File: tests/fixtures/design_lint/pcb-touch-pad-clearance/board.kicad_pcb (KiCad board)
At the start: 2 copper layers, 20 x 20 mm, 1 part, among them J1 Synthetic_Connector

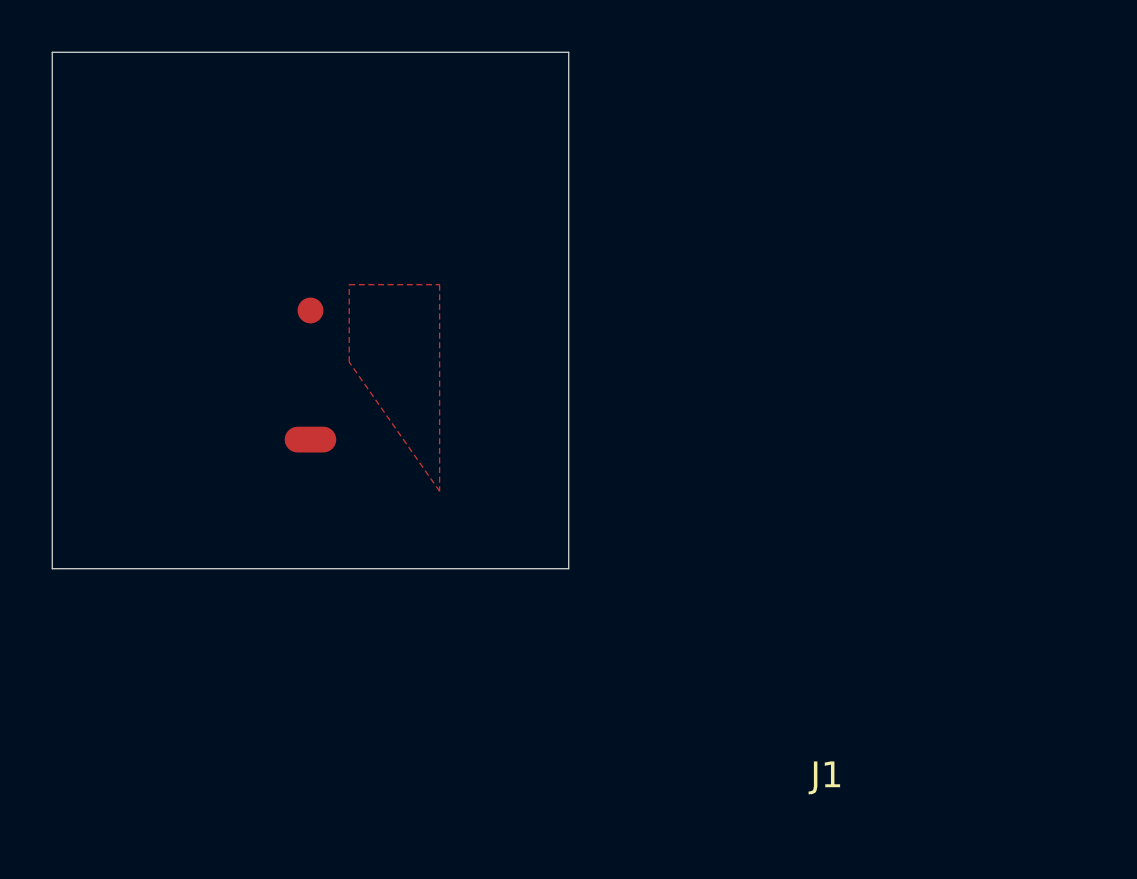
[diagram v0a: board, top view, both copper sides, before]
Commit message: test(lint): cover rotated touch-pad clearance
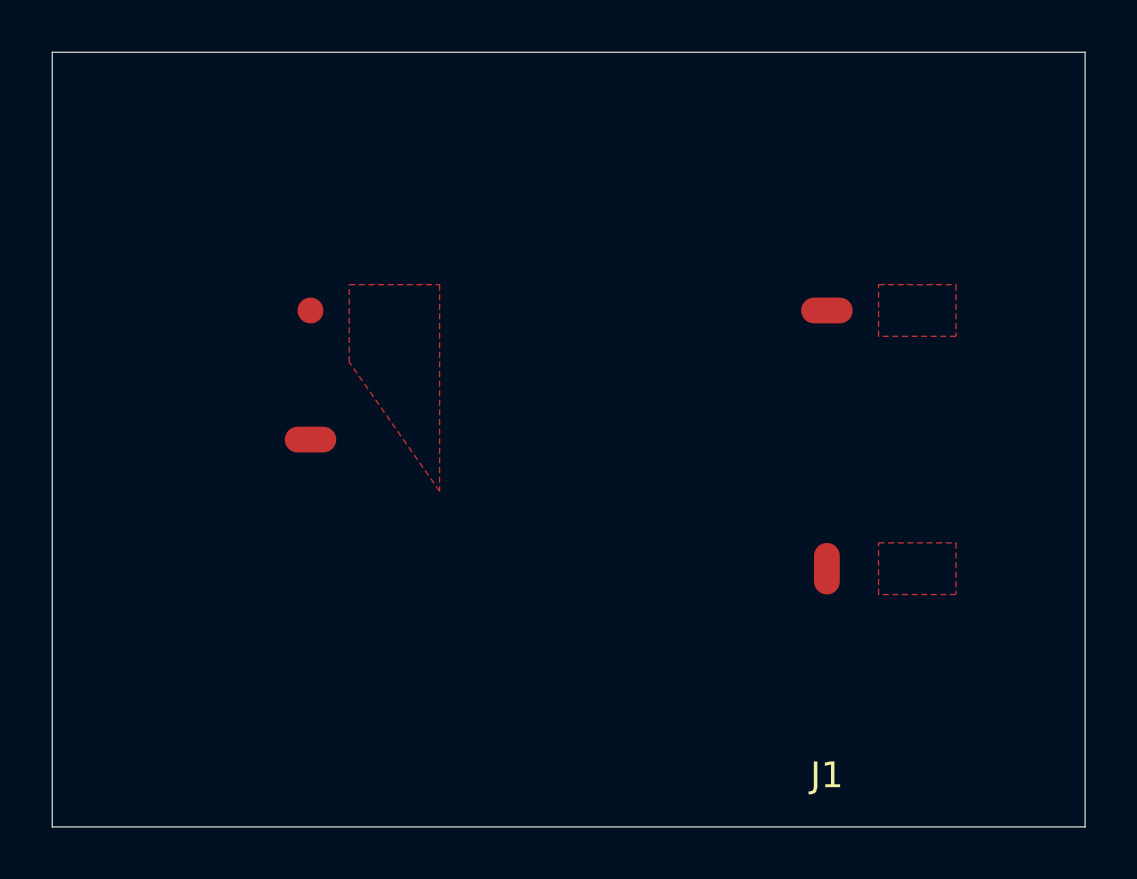
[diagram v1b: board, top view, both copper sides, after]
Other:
- board size 20 x 20 mm -> 40 x 30 mm
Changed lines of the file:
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@@
+      (net 1 "SIGNAL")
+    )
+    (pad "3" smd oval
+      (at 20 0)
+      (size 2 1)
+      (layers "F.Cu" "F.Paste" "F.Mask")
+      (net 1 "SIGNAL")
+    )
+    (pad "4" smd oval
+      (at 20 10 90)
+      (size 2 1)
+      (layers "F.Cu" "F.Paste" "F.Mask")
       (net 1 "SIGNAL")
     )
@@
   (gr_rect
     (start 10 10)
-    (end 30 30)
+    (end 50 40)
     (stroke (width 0.05) (type default))
     (fill none)
@@
       )
     )
+  )
+  (zone
+    (net 2)
+    (net_name "GND")
+    (layers "F.Cu")
+    (name "SYNTHETIC_HORIZONTAL_OVAL_REFERENCE")
+    (hatch edge 0.5)
+    (connect_pads (clearance 0.5))
+    (min_thickness 0.25)
+    (fill yes (thermal_gap 0.5) (thermal_bridge_width 0.5))
+    (polygon
+      (pts
+        (xy 42 19)
+        (xy 45 19)
+        (xy 45 21)
+        (xy 42 21)
+      )
+    )
+  )
+  (zone
+    (net 2)
+    (net_name "GND")
+    (layers "F.Cu")
+    (name "SYNTHETIC_ROTATED_OVAL_REFERENCE")
+    (hatch edge 0.5)
+    (connect_pads (clearance 0.5))
+    (min_thickness 0.25)
+    (fill yes (thermal_gap 0.5) (thermal_bridge_width 0.5))
+    (polygon
+      (pts
+        (xy 42 29)
+        (xy 45 29)
+        (xy 45 31)
+        (xy 42 31)
+      )
+    )
